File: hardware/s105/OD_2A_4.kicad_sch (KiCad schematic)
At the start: 11 parts, among them Q11 BC847C

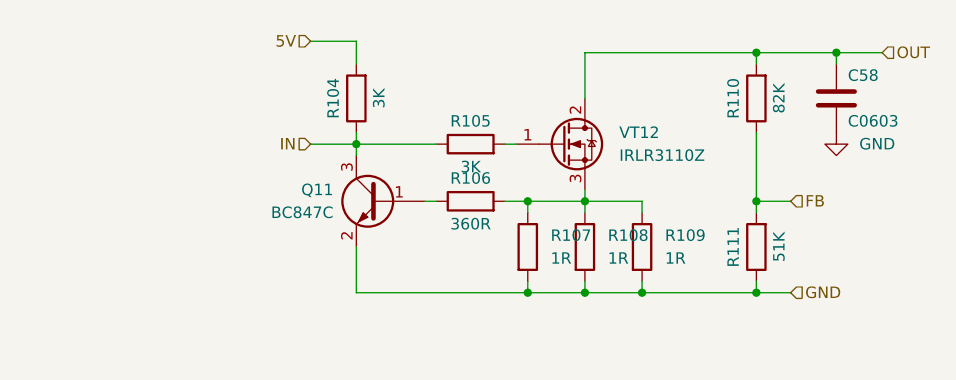
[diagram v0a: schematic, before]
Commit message: вписала в габариты платы, продолжила опознание
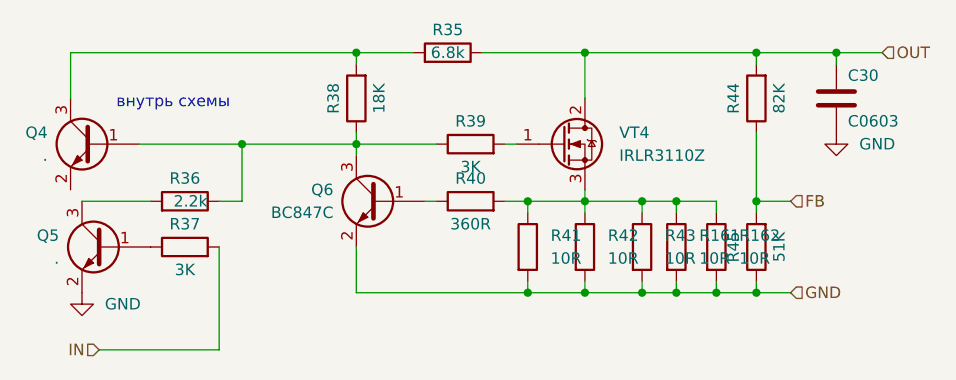
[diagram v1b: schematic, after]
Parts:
- removed C58: C0603, Capacitor_SMD:C_0603_1608Metric, symbol Device:C
- removed Q11: BC847C, Package_TO_SOT_SMD:SOT-23, symbol Transistor_BJT:BC847
- removed R104, R105: 3K, Resistor_SMD:R_0603_1608Metric, symbol Device:R
- removed R106: 360R, Resistor_SMD:R_0603_1608Metric, symbol Device:R
- removed R107, R108, R109: 1R, Resistor_SMD:R_1206_3216Metric, symbol Device:R
- removed R110: 82K, Resistor_SMD:R_0805_2012Metric, symbol Device:R
- removed R111: 51K, Resistor_SMD:R_0603_1608Metric, symbol Device:R
- removed VT12: IRLR3110Z, Package_TO_SOT_SMD:TO-252-2, symbol Transistor_FET:IRFS4115
- added C30: C0603, Capacitor_SMD:C_0603_1608Metric, symbol Device:C
- added Q4, Q5: ., Package_TO_SOT_SMD:SOT-23, symbol Transistor_BJT:BC847
- added Q6: BC847C, Package_TO_SOT_SMD:SOT-23, symbol Transistor_BJT:BC847
- added R161, R162, R41, R42, R43: 10R, Resistor_SMD:R_0805_2012Metric, symbol Device:R
- added R35: 6.8k, Resistor_SMD:R_0805_2012Metric, symbol Device:R
- added R36: 2.2k, Resistor_SMD:R_0805_2012Metric, symbol Device:R
- added R37, R39: 3K, Resistor_SMD:R_0603_1608Metric, symbol Device:R
- added R38: 18K, Resistor_SMD:R_0603_1608Metric, symbol Device:R
- added R40: 360R, Resistor_SMD:R_0603_1608Metric, symbol Device:R
- added R44: 82K, Resistor_SMD:R_0805_2012Metric, symbol Device:R
- added R45: 51K, Resistor_SMD:R_0603_1608Metric, symbol Device:R
- added VT4: IRLR3110Z, Package_TO_SOT_SMD:TO-252-2, symbol Transistor_FET:IRFS4115
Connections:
- net FB: now also R44.1, R45.2
- net GND: now also C30.2, Q5.2 (E), Q6.2 (E), R161.2, R162.2, R41.2, R42.2, R43.2, R45.1
- net IN: now also R37.2
- net OUT: now also C30.1, R35.1, R44.2, VT4.2 (D)
- new net: Q4.1 (B), Q6.3 (C), R36.1, R38.1, R39.1
- new net: Q5.3 (C), R36.2
- new net: R161.1, R162.1, R40.2, R41.1, R42.1, R43.1, VT4.3 (S)
- new net: Q6.1 (B), R40.1
- new net: Q5.1 (B), R37.1
- new net: Q4.3 (C), R35.2, R38.2
- new net: R39.2, VT4.1 (G)
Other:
- note added: "внутрь схемы"

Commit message: закончила пока что
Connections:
- no-connect marks 0 -> 1
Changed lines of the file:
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@@
   (junction (at 161.29 91.44) (diameter 0) (color 0 0 0 0)
   )
+  (no_connect (at 104.14 80.01))
   (wire (pts (xy 154.94 90.17) (xy 154.94 91.44))
     (stroke (width 0) (type default) (color 0 0 0 0))

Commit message: #4 #5 #6 #8
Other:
- company: (none) -> rusEFI
- title: (none) -> s105
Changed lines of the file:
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@@
 (kicad_sch (version 20211123) (generator eeschema)
-  (paper "A4")
+  (paper "A3" portrait)
+  (title_block
+    (title "s105")
+    (rev "0.1")
+    (company "rusEFI")
+  )
   (junction (at 135.89 64.77) (diameter 0) (color 0 0 0 0)
   )
